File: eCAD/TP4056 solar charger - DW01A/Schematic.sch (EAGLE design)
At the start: 33 parts, among them IC1 TP4056X, IC2 DW01A-G, Q1 SI2347DS-T1-GE3, Q2 FS8205A, X1 PV_PANEL, X2 BATTERY, X3 OUTPUT

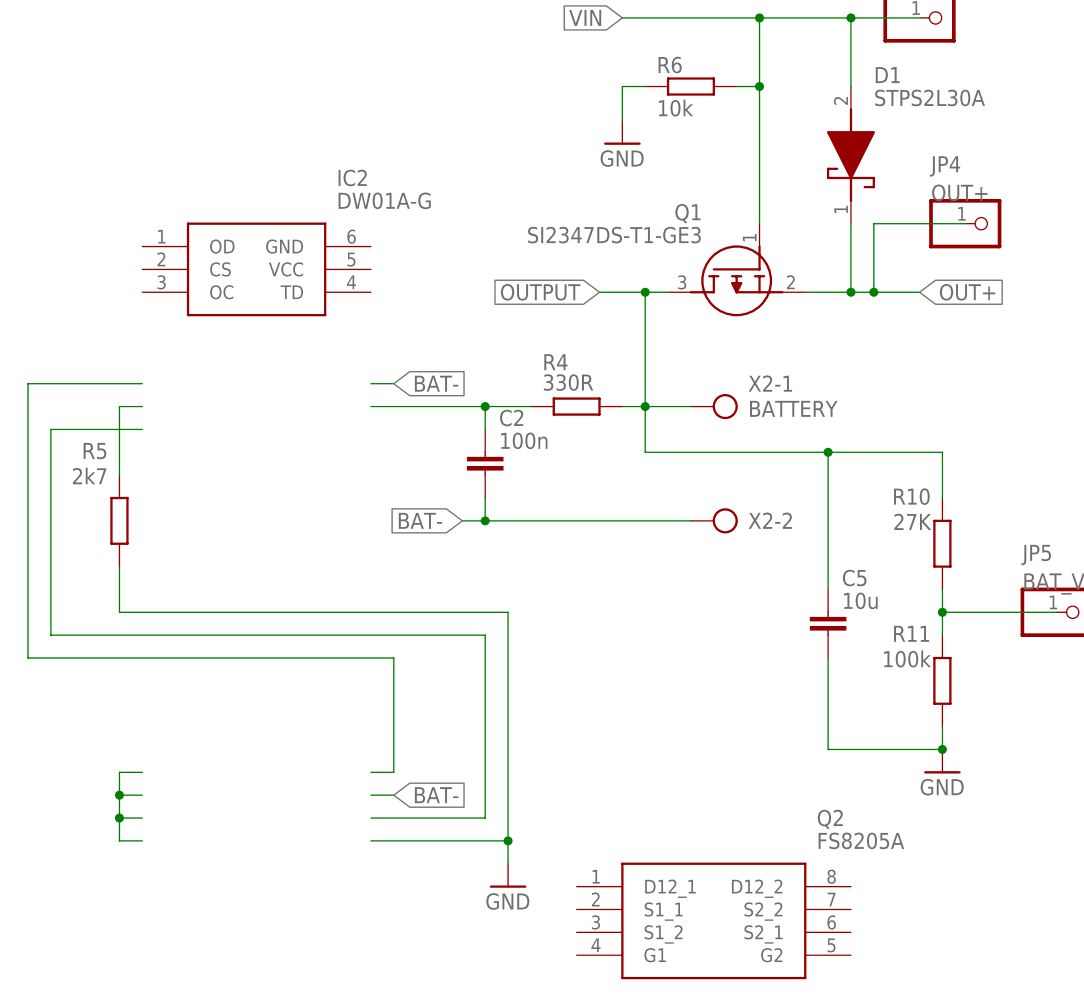
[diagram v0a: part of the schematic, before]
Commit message: DW01A schematic, removed eagle.epf from gitignore
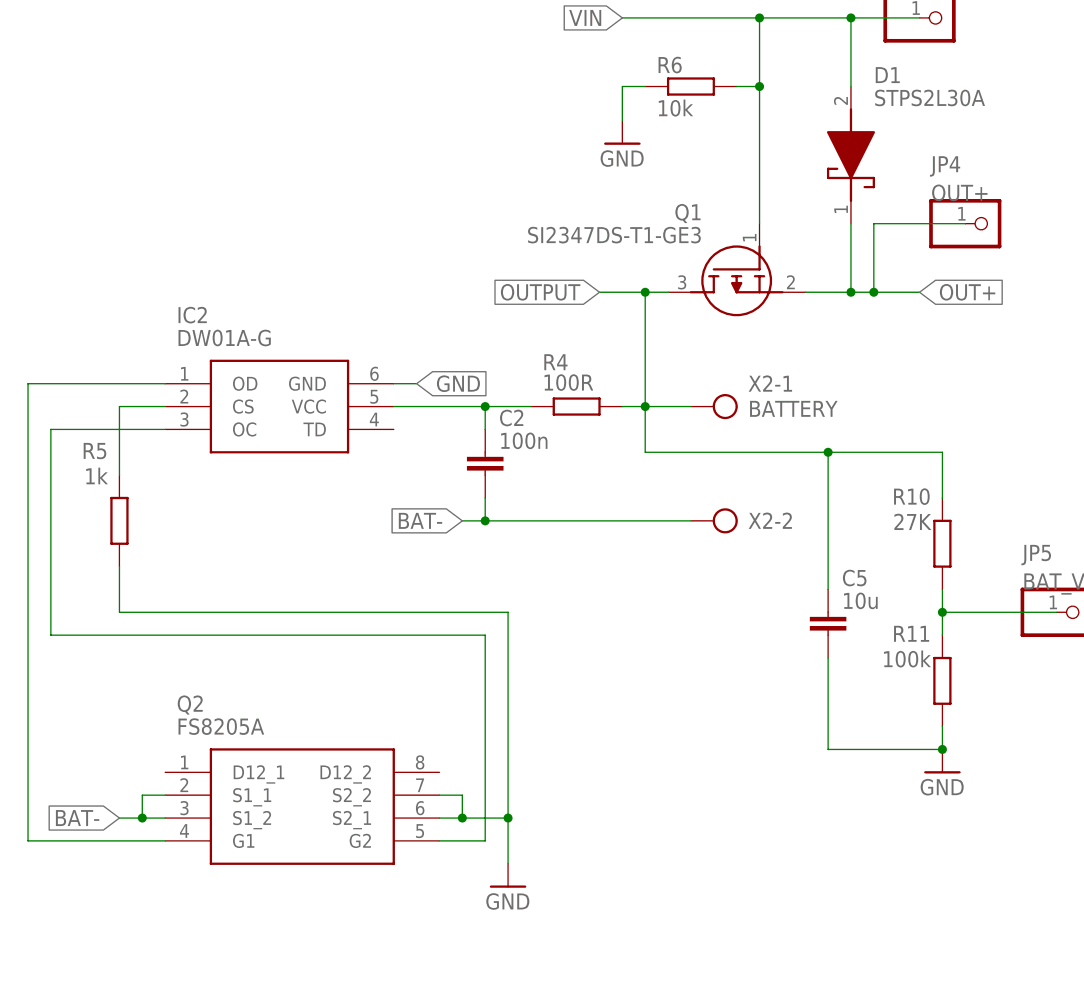
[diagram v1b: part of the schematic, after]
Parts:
- R4: value 330R -> 100R
- R5: value 2k7 -> 1k
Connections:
- new net N$10: IC2.OD, Q2.G1
- new net N$12: IC2.OC, Q2.G2
- net BAT-: now also Q2.S1_1, Q2.S1_2
- net GND: now also IC2.GND, Q2.S2_1, Q2.S2_2
- net N$5: now also IC2.VCC
- net N$9: now also IC2.CS
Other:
- moved on the sheet: IC2, Q2
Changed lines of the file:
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@@
 <setting verticaltext="up"/>
 </settings>
-<grid distance="0.1" unitdist="inch" unit="inch" style="lines" multiple="1" display="no" altdistance="0.01" altunitdist="inch" altunit="inch"/>
+<grid distance="0.1" unitdist="inch" unit="inch" style="lines" multiple="1" display="yes" altdistance="0.01" altunitdist="inch" altunit="inch"/>
 <layers>
 <layer number="1" name="Top" color="4" fill="1" visible="no" active="no"/>
@@
 <part name="GND3" library="supply1" library_urn="urn:adsk.eagle:library:371" deviceset="GND" device=""/>
 <part name="GND4" library="supply1" library_urn="urn:adsk.eagle:library:371" deviceset="GND" device=""/>
-<part name="R4" library="rcl" library_urn="urn:adsk.eagle:library:334" deviceset="R-EU_" device="R0805" package3d_urn="urn:adsk.eagle:package:23553/2" value="330R"/>
-<part name="R5" library="rcl" library_urn="urn:adsk.eagle:library:334" deviceset="R-EU_" device="R0805" package3d_urn="urn:adsk.eagle:package:23553/2" value="2k7"/>
+<part name="R4" library="rcl" library_urn="urn:adsk.eagle:library:334" deviceset="R-EU_" device="R0805" package3d_urn="urn:adsk.eagle:package:23553/2" value="100R"/>
+<part name="R5" library="rcl" library_urn="urn:adsk.eagle:library:334" deviceset="R-EU_" device="R0805" package3d_urn="urn:adsk.eagle:package:23553/2" value="1k"/>
 <part name="C2" library="rcl" library_urn="urn:adsk.eagle:library:334" deviceset="C-EU" device="C0805" package3d_urn="urn:adsk.eagle:package:23617/2" value="100n"/>
 <part name="Q1" library="1-component-search" deviceset="SI2347DS-T1-GE3" device="" override_package3d_urn="urn:adsk.eagle:package:37877156/2" override_package_urn="urn:adsk.eagle:footprint:37877157/1"/>
@@
 <attribute name="VALUE" x="118.11" y="45.72" size="1.778" layer="96"/>
 </instance>
-<instance part="IC2" gate="G$1" x="20.32" y="83.82" smashed="yes">
-<attribute name="NAME" x="41.91" y="91.44" size="1.778" layer="95" align="center-left"/>
-<attribute name="VALUE" x="41.91" y="88.9" size="1.778" layer="96" align="center-left"/>
-</instance>
-<instance part="Q2" gate="G$1" x="68.58" y="12.7" smashed="yes">
-<attribute name="NAME" x="95.25" y="20.32" size="1.778" layer="95" align="center-left"/>
-<attribute name="VALUE" x="95.25" y="17.78" size="1.778" layer="96" align="center-left"/>
+<instance part="IC2" gate="G$1" x="22.86" y="68.58" smashed="yes">
+<attribute name="NAME" x="24.13" y="76.2" size="1.778" layer="95" align="center-left"/>
+<attribute name="VALUE" x="24.13" y="73.66" size="1.778" layer="96" align="center-left"/>
+</instance>
+<instance part="Q2" gate="G$1" x="22.86" y="25.4" smashed="yes">
+<attribute name="NAME" x="24.13" y="33.02" size="1.778" layer="95" align="center-left"/>
+<attribute name="VALUE" x="24.13" y="30.48" size="1.778" layer="96" align="center-left"/>
 </instance>
 </instances>
@@
 <wire x1="17.78" y1="48.26" x2="17.78" y2="43.18" width="0.1524" layer="91"/>
 <wire x1="17.78" y1="43.18" x2="60.96" y2="43.18" width="0.1524" layer="91"/>
-<wire x1="45.72" y1="17.78" x2="60.96" y2="17.78" width="0.1524" layer="91"/>
-<wire x1="60.96" y1="17.78" x2="60.96" y2="43.18" width="0.1524" layer="91"/>
+<wire x1="60.96" y1="15.24" x2="60.96" y2="20.32" width="0.1524" layer="91"/>
 <pinref part="GND6" gate="1" pin="GND"/>
-<wire x1="60.96" y1="15.24" x2="60.96" y2="17.78" width="0.1524" layer="91"/>
-<junction x="60.96" y="17.78"/>
+<wire x1="60.96" y1="20.32" x2="60.96" y2="43.18" width="0.1524" layer="91"/>
+<pinref part="Q2" gate="G$1" pin="S2_1"/>
+<wire x1="53.34" y1="20.32" x2="55.88" y2="20.32" width="0.1524" layer="91"/>
+<junction x="60.96" y="20.32"/>
+<pinref part="Q2" gate="G$1" pin="S2_2"/>
+<wire x1="55.88" y1="20.32" x2="60.96" y2="20.32" width="0.1524" layer="91"/>
+<wire x1="53.34" y1="22.86" x2="55.88" y2="22.86" width="0.1524" layer="91"/>
+<wire x1="55.88" y1="22.86" x2="55.88" y2="20.32" width="0.1524" layer="91"/>
+<junction x="55.88" y="20.32"/>
 </segment>
 <segment>
@@
 <junction x="175.26" y="132.08"/>
 </segment>
+<segment>
+<pinref part="IC2" gate="G$1" pin="GND"/>
+<wire x1="48.26" y1="68.58" x2="50.8" y2="68.58" width="0.1524" layer="91"/>
+<label x="50.8" y="68.58" size="1.778" layer="95" xref="yes"/>
+</segment>
 </net>
 <net name="N$5" class="0">
@@
 <wire x1="63.5" y1="66.04" x2="58.42" y2="66.04" width="0.1524" layer="91"/>
 <pinref part="C2" gate="G$1" pin="1"/>
-<wire x1="58.42" y1="66.04" x2="45.72" y2="66.04" width="0.1524" layer="91"/>
 <wire x1="58.42" y1="63.5" x2="58.42" y2="66.04" width="0.1524" layer="91"/>
+<pinref part="IC2" gate="G$1" pin="VCC"/>
+<wire x1="58.42" y1="66.04" x2="48.26" y2="66.04" width="0.1524" layer="91"/>
 <junction x="58.42" y="66.04"/>
 </segment>
@@
 <net name="N$9" class="0">
 <segment>
-<wire x1="20.32" y1="66.04" x2="17.78" y2="66.04" width="0.1524" layer="91"/>
 <pinref part="R5" gate="G$1" pin="2"/>
 <wire x1="17.78" y1="66.04" x2="17.78" y2="58.42" width="0.1524" layer="91"/>
+<pinref part="IC2" gate="G$1" pin="CS"/>
+<wire x1="22.86" y1="66.04" x2="17.78" y2="66.04" width="0.1524" layer="91"/>
 </segment>
 </net>
 <net name="N$10" class="0">
 <segment>
-<wire x1="45.72" y1="25.4" x2="48.26" y2="25.4" width="0.1524" layer="91"/>
-<wire x1="48.26" y1="25.4" x2="48.26" y2="38.1" width="0.1524" layer="91"/>
-<wire x1="48.26" y1="38.1" x2="7.62" y2="38.1" width="0.1524" layer="91"/>
-<wire x1="7.62" y1="38.1" x2="7.62" y2="68.58" width="0.1524" layer="91"/>
-<wire x1="7.62" y1="68.58" x2="20.32" y2="68.58" width="0.1524" layer="91"/>
+<wire x1="7.62" y1="17.78" x2="7.62" y2="68.58" width="0.1524" layer="91"/>
+<pinref part="IC2" gate="G$1" pin="OD"/>
+<wire x1="22.86" y1="68.58" x2="7.62" y2="68.58" width="0.1524" layer="91"/>
+<pinref part="Q2" gate="G$1" pin="G1"/>
+<wire x1="7.62" y1="17.78" x2="22.86" y2="17.78" width="0.1524" layer="91"/>
 </segment>
 </net>
 <net name="N$12" class="0">
 <segment>
-<wire x1="45.72" y1="20.32" x2="58.42" y2="20.32" width="0.1524" layer="91"/>
-<wire x1="58.42" y1="20.32" x2="58.42" y2="40.64" width="0.1524" layer="91"/>
 <wire x1="58.42" y1="40.64" x2="10.16" y2="40.64" width="0.1524" layer="91"/>
 <wire x1="10.16" y1="40.64" x2="10.16" y2="63.5" width="0.1524" layer="91"/>
-<wire x1="10.16" y1="63.5" x2="20.32" y2="63.5" width="0.1524" layer="91"/>
-</segment>
-</net>
-<net name="N$13" class="0">
-<segment>
-<wire x1="20.32" y1="25.4" x2="17.78" y2="25.4" width="0.1524" layer="91"/>
-<wire x1="17.78" y1="25.4" x2="17.78" y2="22.86" width="0.1524" layer="91"/>
-<wire x1="17.78" y1="22.86" x2="17.78" y2="20.32" width="0.1524" layer="91"/>
-<wire x1="17.78" y1="20.32" x2="17.78" y2="17.78" width="0.1524" layer="91"/>
-<wire x1="17.78" y1="17.78" x2="20.32" y2="17.78" width="0.1524" layer="91"/>
-<wire x1="20.32" y1="20.32" x2="17.78" y2="20.32" width="0.1524" layer="91"/>
-<junction x="17.78" y="20.32"/>
-<wire x1="20.32" y1="22.86" x2="17.78" y2="22.86" width="0.1524" layer="91"/>
-<junction x="17.78" y="22.86"/>
+<pinref part="IC2" gate="G$1" pin="OC"/>
+<wire x1="22.86" y1="63.5" x2="10.16" y2="63.5" width="0.1524" layer="91"/>
+<wire x1="58.42" y1="40.64" x2="58.42" y2="17.78" width="0.1524" layer="91"/>
+<pinref part="Q2" gate="G$1" pin="G2"/>
+<wire x1="58.42" y1="17.78" x2="53.34" y2="17.78" width="0.1524" layer="91"/>
 </segment>
 </net>
@@
 <net name="BAT-" class="0">
 <segment>
-<wire x1="45.72" y1="68.58" x2="48.26" y2="68.58" width="0.1524" layer="91"/>
-<label x="48.26" y="68.58" size="1.778" layer="95" xref="yes"/>
-</segment>
-<segment>
-<wire x1="45.72" y1="22.86" x2="48.26" y2="22.86" width="0.1524" layer="91"/>
-<label x="48.26" y="22.86" size="1.778" layer="95" xref="yes"/>
-</segment>
-<segment>
 <pinref part="C2" gate="G$1" pin="2"/>
 <wire x1="58.42" y1="53.34" x2="58.42" y2="55.88" width="0.1524" layer="91"/>
@@
 <junction x="58.42" y="53.34"/>
 </segment>
-</net>
+<segment>
+<pinref part="Q2" gate="G$1" pin="S1_1"/>
+<wire x1="22.86" y1="22.86" x2="20.32" y2="22.86" width="0.1524" layer="91"/>
+<wire x1="20.32" y1="22.86" x2="20.32" y2="20.32" width="0.1524" layer="91"/>
+<pinref part="Q2" gate="G$1" pin="S1_2"/>
+<wire x1="20.32" y1="20.32" x2="22.86" y2="20.32" width="0.1524" layer="91"/>
+<wire x1="20.32" y1="20.32" x2="17.78" y2="20.32" width="0.1524" layer="91"/>
+<junction x="20.32" y="20.32"/>
+<label x="17.78" y="20.32" size="1.778" layer="95" rot="R180" xref="yes"/>
+</segment>
+</net>

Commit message: Created version of charger with JLC stock parts
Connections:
- net BAT-: now also IC2.GND
- net GND: no longer IC2.GND
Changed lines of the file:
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@@
 <setting verticaltext="up"/>
 </settings>
-<grid distance="0.1" unitdist="inch" unit="inch" style="lines" multiple="1" display="yes" altdistance="0.01" altunitdist="inch" altunit="inch"/>
+<grid distance="0.1" unitdist="inch" unit="inch" style="lines" multiple="1" display="no" altdistance="0.01" altunitdist="inch" altunit="inch"/>
 <layers>
 <layer number="1" name="Top" color="4" fill="1" visible="no" active="no"/>
@@
 <junction x="175.26" y="132.08"/>
 </segment>
-<segment>
-<pinref part="IC2" gate="G$1" pin="GND"/>
-<wire x1="48.26" y1="68.58" x2="50.8" y2="68.58" width="0.1524" layer="91"/>
-<label x="50.8" y="68.58" size="1.778" layer="95" xref="yes"/>
-</segment>
 </net>
 <net name="N$5" class="0">
@@
 <label x="17.78" y="20.32" size="1.778" layer="95" rot="R180" xref="yes"/>
 </segment>
-</net>
+<segment>
+<pinref part="IC2" gate="G$1" pin="GND"/>
+<wire x1="48.26" y1="68.58" x2="50.8" y2="68.58" width="0.1524" layer="91"/>
+<label x="50.8" y="68.58" size="1.778" layer="95" xref="yes"/>
+</segment>
+</net>

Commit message: Added power circuits, connection to Quectel devkit
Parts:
- removed JP4: OUT+, pinhead:PINHD-1X1
- removed PS1: BU33SD5WG-TR, 1-component-search:BU33SD5WG-TR
- added IC3: ME6211C33M5G-N, 1-component-search:ME6211C33M5G-N
- C3, C4: value 470n -> 1u
- D1: value STPS2L30A -> 1N4148WS-7-F; device 1-component-search:STPS2L30A -> 1-component-search:1N4148WS-7-F
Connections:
- net GND: now also IC3.VSS; no longer PS1.GND
- net N$14: now also IC3.VOUT; no longer PS1.VOUT
- net OUT+: now also IC3.CE, IC3.VIN; no longer JP4.1, PS1.STBY, PS1.VIN
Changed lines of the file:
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@@
 <part name="C2" library="rcl" library_urn="urn:adsk.eagle:library:334" deviceset="C-EU" device="C0805" package3d_urn="urn:adsk.eagle:package:23617/2" value="100n"/>
 <part name="Q1" library="1-component-search" deviceset="SI2347DS-T1-GE3" device="" override_package3d_urn="urn:adsk.eagle:package:37877156/2" override_package_urn="urn:adsk.eagle:footprint:37877157/1"/>
-<part name="D1" library="1-component-search" deviceset="STPS2L30A" device="" override_package3d_urn="urn:adsk.eagle:package:37877152/2" override_package_urn="urn:adsk.eagle:footprint:37877153/1"/>
 <part name="R6" library="rcl" library_urn="urn:adsk.eagle:library:334" deviceset="R-EU_" device="R0805" package3d_urn="urn:adsk.eagle:package:23553/2" value="10k"/>
 <part name="GND7" library="supply1" library_urn="urn:adsk.eagle:library:371" deviceset="GND" device=""/>
@@
 <part name="X2" library="con-ptr500" library_urn="urn:adsk.eagle:library:181" deviceset="AK300/2" device="" package3d_urn="urn:adsk.eagle:package:9881/1" value="BATTERY"/>
 <part name="GND5" library="supply1" library_urn="urn:adsk.eagle:library:371" deviceset="GND" device=""/>
-<part name="PS1" library="1-component-search" deviceset="BU33SD5WG-TR" device="" override_package3d_urn="urn:adsk.eagle:package:37877144/2" override_package_urn="urn:adsk.eagle:footprint:37877145/1"/>
-<part name="C3" library="rcl" library_urn="urn:adsk.eagle:library:334" deviceset="C-EU" device="C0805" package3d_urn="urn:adsk.eagle:package:23617/2" value="470n"/>
-<part name="C4" library="rcl" library_urn="urn:adsk.eagle:library:334" deviceset="C-EU" device="C0805" package3d_urn="urn:adsk.eagle:package:23617/2" value="470n"/>
+<part name="C3" library="rcl" library_urn="urn:adsk.eagle:library:334" deviceset="C-EU" device="C0805" package3d_urn="urn:adsk.eagle:package:23617/2" value="1u"/>
+<part name="C4" library="rcl" library_urn="urn:adsk.eagle:library:334" deviceset="C-EU" device="C0805" package3d_urn="urn:adsk.eagle:package:23617/2" value="1u"/>
 <part name="GND9" library="supply1" library_urn="urn:adsk.eagle:library:371" deviceset="GND" device=""/>
 <part name="GND10" library="supply1" library_urn="urn:adsk.eagle:library:371" deviceset="GND" device=""/>
@@
 <attribute name="SPICEPREFIX" value="X"/>
 </part>
-<part name="JP4" library="pinhead" library_urn="urn:adsk.eagle:library:325" deviceset="PINHD-1X1" device="" package3d_urn="urn:adsk.eagle:package:22485/2" value="OUT+"/>
 <part name="JP5" library="pinhead" library_urn="urn:adsk.eagle:library:325" deviceset="PINHD-1X1" device="" package3d_urn="urn:adsk.eagle:package:22485/2" value="BAT_V"/>
 <part name="IC2" library="1-component-search" deviceset="DW01A-G" device=""/>
 <part name="Q2" library="1-component-search" deviceset="FS8205A" device=""/>
+<part name="IC3" library="1-component-search" deviceset="ME6211C33M5G-N" device=""/>
+<part name="D1" library="1-component-search" deviceset="1N4148WS-7-F" device=""/>
 </parts>
 <sheets>
@@
 <attribute name="VALUE" x="82.55" y="85.09" size="1.778" layer="96" rot="MR0" align="center-left"/>
 </instance>
-<instance part="D1" gate="G$1" x="99.06" y="83.82" smashed="yes" rot="R90">
-<attribute name="NAME" x="101.6" y="102.87" size="1.778" layer="95" align="center-left"/>
-<attribute name="VALUE" x="101.6" y="100.33" size="1.778" layer="96" align="center-left"/>
-</instance>
 <instance part="R6" gate="G$1" x="81.28" y="101.6" smashed="yes">
 <attribute name="NAME" x="77.47" y="103.0986" size="1.778" layer="95"/>
@@
 <attribute name="VALUE" x="139.7" y="106.68" size="1.778" layer="96"/>
 </instance>
-<instance part="PS1" gate="G$1" x="177.8" y="66.04" smashed="yes">
-<attribute name="NAME" x="179.07" y="73.66" size="1.778" layer="95" align="center-left"/>
-<attribute name="VALUE" x="179.07" y="71.12" size="1.778" layer="96" align="center-left"/>
-</instance>
 <instance part="C3" gate="G$1" x="162.56" y="55.88" smashed="yes">
 <attribute name="NAME" x="164.084" y="58.801" size="1.778" layer="95"/>
@@
 <attribute name="VALUE" x="102.87" y="111.76" size="1.778" layer="96"/>
 </instance>
-<instance part="JP4" gate="G$1" x="114.3" y="86.36" smashed="yes">
-<attribute name="NAME" x="107.95" y="92.075" size="1.778" layer="95"/>
-<attribute name="VALUE" x="107.95" y="88.9" size="1.778" layer="96"/>
-</instance>
 <instance part="JP5" gate="G$1" x="124.46" y="43.18" smashed="yes">
 <attribute name="NAME" x="118.11" y="48.895" size="1.778" layer="95"/>
@@
 <attribute name="NAME" x="24.13" y="33.02" size="1.778" layer="95" align="center-left"/>
 <attribute name="VALUE" x="24.13" y="30.48" size="1.778" layer="96" align="center-left"/>
+</instance>
+<instance part="IC3" gate="G$1" x="177.8" y="66.04" smashed="yes">
+<attribute name="NAME" x="179.07" y="73.66" size="1.778" layer="95" align="center-left"/>
+<attribute name="VALUE" x="179.07" y="71.12" size="1.778" layer="96" align="center-left"/>
+</instance>
+<instance part="D1" gate="G$1" x="99.06" y="86.36" smashed="yes" rot="R90">
+<attribute name="NAME" x="100.33" y="101.6" size="1.778" layer="95" align="center-left"/>
+<attribute name="VALUE" x="100.33" y="99.06" size="1.778" layer="96" align="center-left"/>
 </instance>
 </instances>
@@
 </segment>
 <segment>
-<pinref part="PS1" gate="G$1" pin="GND"/>
 <wire x1="177.8" y1="63.5" x2="175.26" y2="63.5" width="0.1524" layer="91"/>
 <wire x1="175.26" y1="63.5" x2="175.26" y2="45.72" width="0.1524" layer="91"/>
 <pinref part="GND9" gate="1" pin="GND"/>
+<pinref part="IC3" gate="G$1" pin="VSS"/>
 </segment>
 <segment>
@@
 <segment>
 <pinref part="Q1" gate="G$1" pin="S"/>
-<wire x1="106.68" y1="78.74" x2="101.6" y2="78.74" width="0.1524" layer="91"/>
-<pinref part="D1" gate="G$1" pin="K"/>
-<wire x1="101.6" y1="78.74" x2="99.06" y2="78.74" width="0.1524" layer="91"/>
+<wire x1="106.68" y1="78.74" x2="99.06" y2="78.74" width="0.1524" layer="91"/>
 <wire x1="99.06" y1="78.74" x2="93.98" y2="78.74" width="0.1524" layer="91"/>
 <wire x1="99.06" y1="86.36" x2="99.06" y2="78.74" width="0.1524" layer="91"/>
 <junction x="99.06" y="78.74"/>
 <label x="106.68" y="78.74" size="1.778" layer="95" xref="yes"/>
-<pinref part="JP4" gate="G$1" pin="1"/>
-<wire x1="111.76" y1="86.36" x2="101.6" y2="86.36" width="0.1524" layer="91"/>
-<wire x1="101.6" y1="86.36" x2="101.6" y2="78.74" width="0.1524" layer="91"/>
-<junction x="101.6" y="78.74"/>
-</segment>
-<segment>
-<pinref part="PS1" gate="G$1" pin="VIN"/>
+<pinref part="D1" gate="G$1" pin="K"/>
+</segment>
+<segment>
 <wire x1="177.8" y1="66.04" x2="170.18" y2="66.04" width="0.1524" layer="91"/>
-<pinref part="PS1" gate="G$1" pin="STBY"/>
 <wire x1="170.18" y1="66.04" x2="162.56" y2="66.04" width="0.1524" layer="91"/>
 <wire x1="162.56" y1="66.04" x2="154.94" y2="66.04" width="0.1524" layer="91"/>
@@
 <junction x="162.56" y="66.04"/>
 <label x="154.94" y="66.04" size="1.778" layer="95" rot="R180" xref="yes"/>
+<pinref part="IC3" gate="G$1" pin="VIN"/>
+<pinref part="IC3" gate="G$1" pin="CE"/>
 </segment>
 </net>
@@
 </segment>
 <segment>
-<pinref part="D1" gate="G$1" pin="A"/>
 <wire x1="99.06" y1="101.6" x2="99.06" y2="109.22" width="0.1524" layer="91"/>
 <wire x1="99.06" y1="109.22" x2="88.9" y2="109.22" width="0.1524" layer="91"/>
@@
 <wire x1="106.68" y1="109.22" x2="99.06" y2="109.22" width="0.1524" layer="91"/>
 <junction x="99.06" y="109.22"/>
+<pinref part="D1" gate="G$1" pin="A"/>
 </segment>
 </net>
 <net name="N$14" class="0">
 <segment>
-<pinref part="PS1" gate="G$1" pin="VOUT"/>
 <wire x1="205.74" y1="63.5" x2="210.82" y2="63.5" width="0.1524" layer="91"/>
 <pinref part="C4" gate="G$1" pin="1"/>
@@
 <junction x="210.82" y="63.5"/>
 <pinref part="X3" gate="-1" pin="KL"/>
-</segment>
-</net>
+<pinref part="IC3" gate="G$1" pin="VOUT"/>
+</segment>
+</net>
